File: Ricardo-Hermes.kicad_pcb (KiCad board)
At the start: 4 copper layers, 42.8 x 63.6 mm, 147 parts, among them IC2 SX1280, J1 RBUS, J2 USB_C_Receptacle_USB2.0, J3 Conn_01x03_Pin, J4 Conn_01x03_Pin, U1 ESP32-S3, U11 SC4215ASTRT, U12 SKY66112-11, U13 DEA202450BT-1213C1, U2 SN65HVD230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

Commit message: Silkscreen WIP
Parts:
- removed the G*** at (141.7, 116.0)
- added G***: LOGO, iclr:Terraria, B.Cu at (144.1, 131.5)
- moved R31 0.53 mm to (139.8, 114.0)
- moved G*** 0.26 mm to (128.4, 130.7)
- moved R32 0.22 mm to (139.8, 113.0)
- moved G*** 0.15 mm to (135.1, 130.8)
- renumbered POWER_UART1 to P_UART
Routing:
- net GND: track 329.7 -> 330.7 mm
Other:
- board text removed: "Hermes, the winged herald, swift as thought and nimble as shadows, carrying the will of gods to the ears of mortals."
- board text removed: "Silkscreen shows which signals the test points represent on the front"

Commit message: Final changes
Art and BOM still need to be done
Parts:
- moved R12 0.48 mm to (151.6, 80.0)
- moved D+_TP1 0.29 mm to (152.1, 82.0)
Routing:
- net +VDC: track 33.4 -> 35.4 mm
- net VBUS: track 39.2 -> 40.6 mm

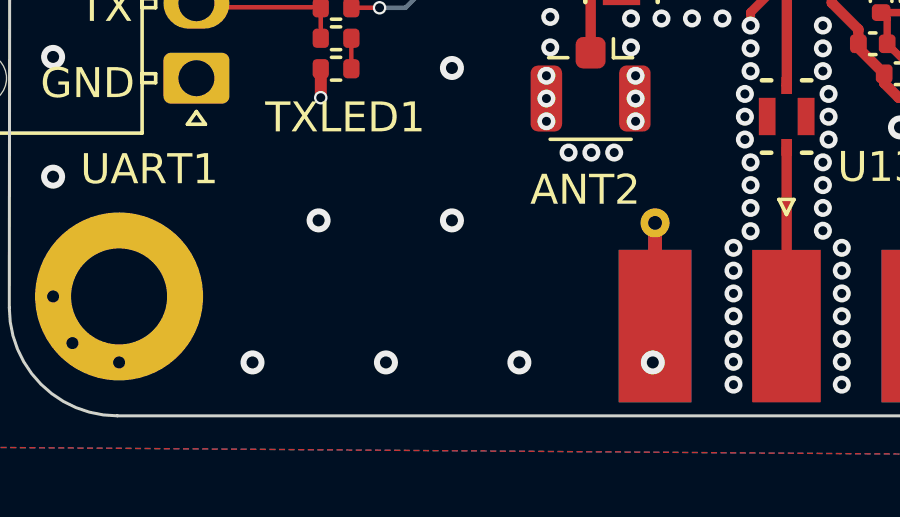
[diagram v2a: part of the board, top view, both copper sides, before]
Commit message: Silkscreen changes
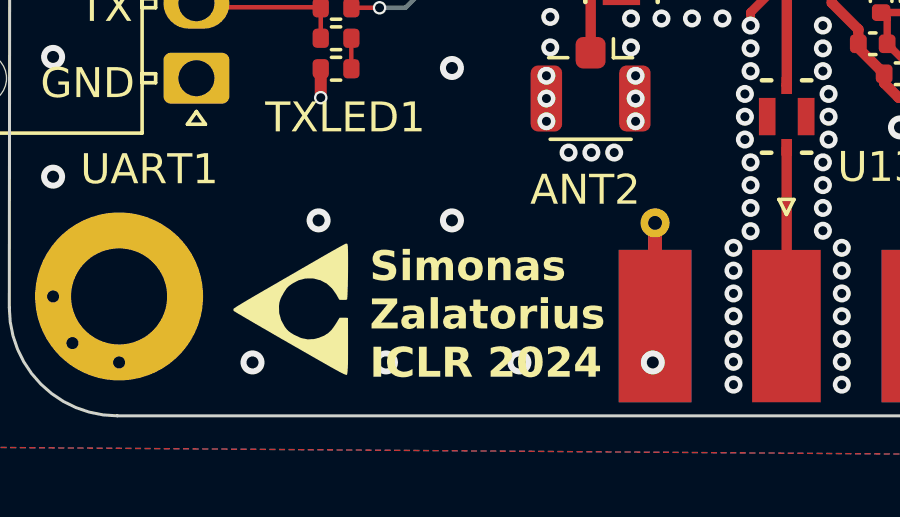
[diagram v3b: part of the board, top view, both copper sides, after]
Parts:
- added G***: LOGO, iclr:trilogo, F.Cu at (128.6, 130.8)
- added G***: LOGO, iclr:HermesArt, B.Cu at (139.9, 99.4)
- G***: moved to F.Cu
- moved G*** 0.48 mm to (144.6, 131.5), turned to 0 degrees
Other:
- board text added: "Hermes"
- board text added: "Simonas Zalatorius ICLR 2024"
- board text added: "V1"
- board text removed: "Hermes V1"

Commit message: Post Review changes, more to come...
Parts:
- removed CS1, MISO1, MOSI1, SCK1: TestPoint, TestPoint:TestPoint_Pad_D1.0mm
- moved R25 11.2 mm to (141.1, 101.3), turned to 90 degrees
- moved R30 10.6 mm to (144.1, 101.3), turned to 90 degrees
- moved R26 10.6 mm to (142.1, 101.3), turned to 90 degrees
- moved R29 10.4 mm to (143.1, 101.3), turned to 90 degrees
- moved R35 5.95 mm to (135.0, 106.7)
- moved C16 5.30 mm to (126.6, 86.1), turned to 0 degrees
- moved C15 4.65 mm to (124.7, 86.1), turned to 180 degrees
- moved C5 4.00 mm to (136.0, 101.7), turned to 180 degrees
- moved DIO2 3.47 mm to (148.2, 101.0)
- moved R38 3.27 mm to (147.3, 103.9)
- moved C4 2.11 mm to (136.0, 102.8)
- moved C9 2.11 mm to (137.3, 99.6)
- moved L4 1.96 mm to (142.9, 107.1)
- moved C54 1.91 mm to (146.0, 106.4)
- moved C57 1.87 mm to (145.0, 106.9)
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- renumbered P_UART to POWER_UART1
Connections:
- CHL1 pad 1: CHL -> CTX
- CTX1 pad 1: CTX -> CHL
- R25 pad 2: Net-(U1-SPICS0/GPIO29) -> Net-(U1-GPIO1/ADC1_CH0)
- R26 pad 2: Net-(U1-SPICLK/GPIO30) -> Net-(U1-GPIO2/ADC1_CH1)
- R29 pad 2: Net-(U1-SPIQ/GPIO31) -> Net-(U1-GPIO4/ADC1_CH3)
- R30 pad 2: Net-(U1-SPID/GPIO32) -> Net-(U1-GPIO5/ADC1_CH4)
- U1 pad 10: DIO3 -> Net-(U1-GPIO5/ADC1_CH4)
- U1 pad 11: DIO1 -> unconnected-(U1-GPIO6/ADC1_CH5-Pad11)
- U1 pad 12: SX_BUSY -> DIO3
- U1 pad 13: unconnected-(U1-GPIO8/ADC1_CH7-Pad13) -> DIO2
- U1 pad 14: unconnected-(U1-GPIO9/ADC1_CH8-Pad14) -> DIO1
- U1 pad 15: unconnected-(U1-GPIO10/ADC1_CH9-Pad15) -> SX_BUSY
- U1 pad 17: CTX -> CHL
- U1 pad 18: CHL -> CTX
- U1 pad 32: Net-(U1-SPICS0/GPIO29) -> unconnected-(U1-SPICS0/GPIO29-Pad32)
- U1 pad 33: Net-(U1-SPICLK/GPIO30) -> unconnected-(U1-SPICLK/GPIO30-Pad33)
- U1 pad 34: Net-(U1-SPIQ/GPIO31) -> unconnected-(U1-SPIQ/GPIO31-Pad34)
- U1 pad 35: Net-(U1-SPID/GPIO32) -> unconnected-(U1-SPID/GPIO32-Pad35)
- U1 pad 6: unconnected-(U1-GPIO1/ADC1_CH0-Pad6) -> Net-(U1-GPIO1/ADC1_CH0)
- U1 pad 7: unconnected-(U1-GPIO2/ADC1_CH1-Pad7) -> Net-(U1-GPIO2/ADC1_CH1)
- U1 pad 9: DIO2 -> Net-(U1-GPIO4/ADC1_CH3)
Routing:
- net CS: track 34.1 -> 16.6 mm, vias 2 -> 0
- net SCK: track 31.8 -> 15.4 mm, vias 2 -> 0
- net MOSI: track 28.8 -> 14.4 mm, vias 2 -> 0
- net MISO: track 26.0 -> 13.3 mm, vias 2 -> 0
- net VAA: track 60.3 -> 50.0 mm
- net CHL: track 40.9 -> 32.9 mm
- net VDDF: track 26.6 -> 32.9 mm, vias 2 -> 3
- net SX_BUSY: track 15.5 -> 10.0 mm, vias 2 -> 1
- net GND: track 330.9 -> 326.9 mm, vias 189 -> 200
- net CPS: track 39.4 -> 36.8 mm
- net +3V3: track 129.2 -> 131.5 mm, vias 9 -> 10
- net CRX: track 41.4 -> 43.6 mm
- net ANT_SEL: track 47.5 -> 49.5 mm
- net CTX: track 36.0 -> 34.0 mm
- net Net-(U1-SPICS0/GPIO29): track 1.95 -> 0.00 mm
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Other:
- board text added: "Simonas Zalatorius ICLR 2024 Electronics"
- board text removed: "Simonas Zalatorius ICLR 2024"

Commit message: Tidying up
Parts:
- moved DIO1 4.21 mm to (153.5, 101.0)
- moved RXD_1 2.62 mm to (152.0, 104.3)
- moved R36 1.96 mm to (149.6, 103.3), turned to 0 degrees
- moved R37 1.30 mm to (149.6, 104.3)
- moved TXD_1 1.05 mm to (152.0, 103.3)
- moved H1 0.44 mm to (121.7, 74.6)
- moved H3 0.42 mm to (121.7, 130.6)
- moved ANT1 0.40 mm to (145.8, 129.5)
- moved R38 0.19 mm to (147.2, 103.8)
- moved D-_TP1 0.18 mm to (152.1, 88.2)
- moved DIO3_D1 0.14 mm to (146.2, 103.8)
- moved H2 0.12 mm to (157.7, 74.6)
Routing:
- net SX_BUSY: track 10.0 -> 14.6 mm, vias 1 -> 2
- net GND: track 326.9 -> 330.7 mm, vias 200 -> 201
- net +3V3: track 131.5 -> 128.9 mm
- net VAA: track 50.0 -> 51.0 mm
- net DIO1: track 19.9 -> 19.1 mm, vias 1 -> 0
- net DIO3: track 13.3 -> 14.0 mm
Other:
- board size 42.8 x 63.6 mm -> 43 x 63 mm
- board text added: "JLCJLCJLCJLC"
